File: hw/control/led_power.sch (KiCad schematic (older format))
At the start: 23 parts, among them Q1001 BC807, Q1002 BC817, U801 LM2678T-ADJ

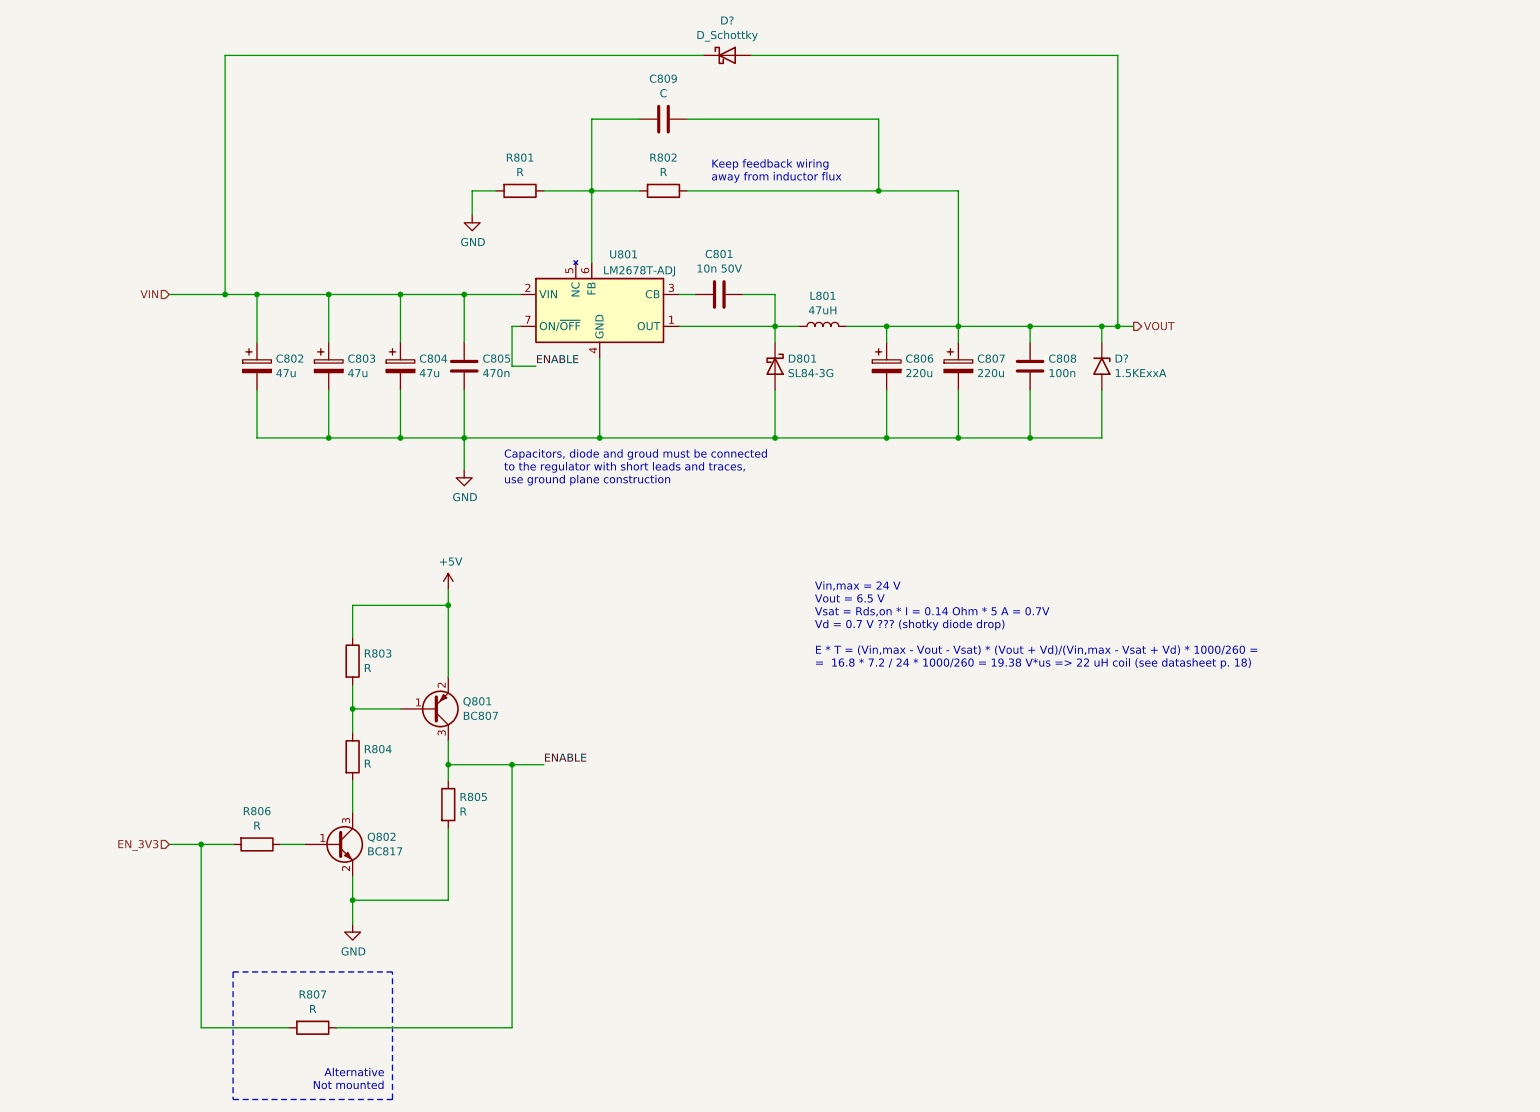
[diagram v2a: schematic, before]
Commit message: [hw] Assign control board footprints
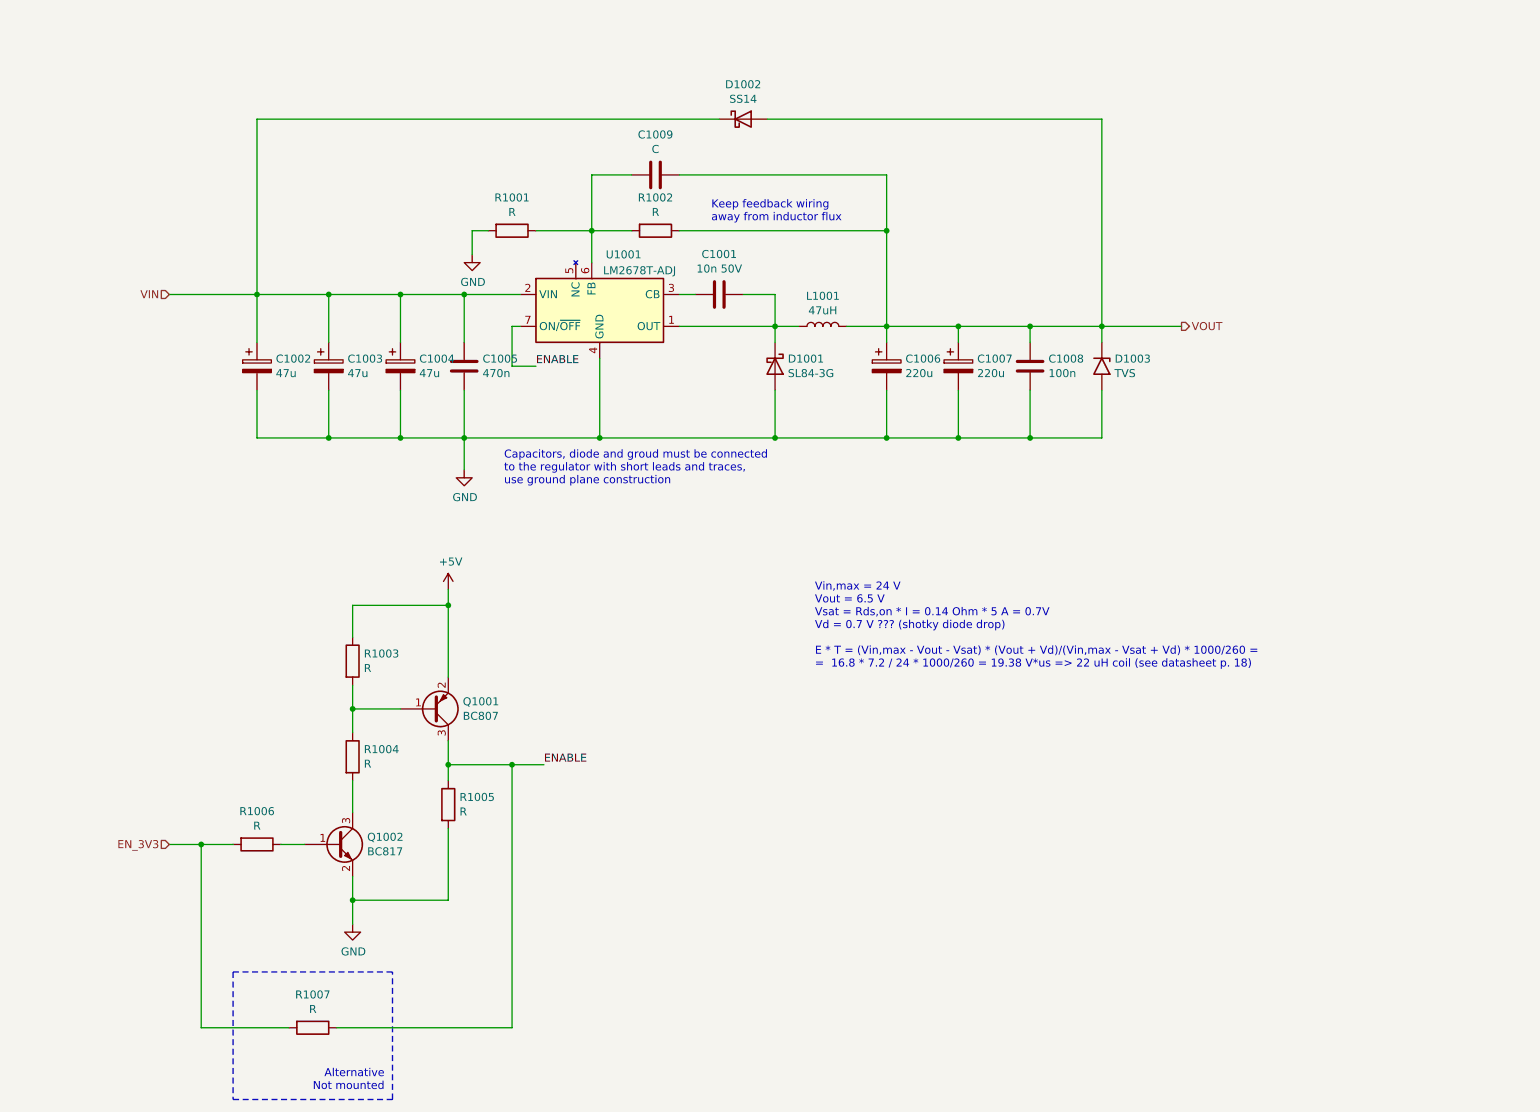
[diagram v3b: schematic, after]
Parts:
- C809: footprint (none) -> Capacitor_SMD:C_0805_2012Metric_Pad1.18x1.45mm_HandSolder
- D802: renamed from D?; value D_Schottky -> SS14; footprint (none) -> Diode_SMD:D_SMA-SMB_Universal_Handsoldering
- D803: renamed from D?; value 1.5KExxA -> TVS; footprint Diode_THT:D_DO-201AE_P15.24mm_Horizontal -> Diode_SMD:D_SMA_Handsoldering
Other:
- moved on the sheet: C1009, D1002, R1001, R1002

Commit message: [hw] Calculate some values in control board
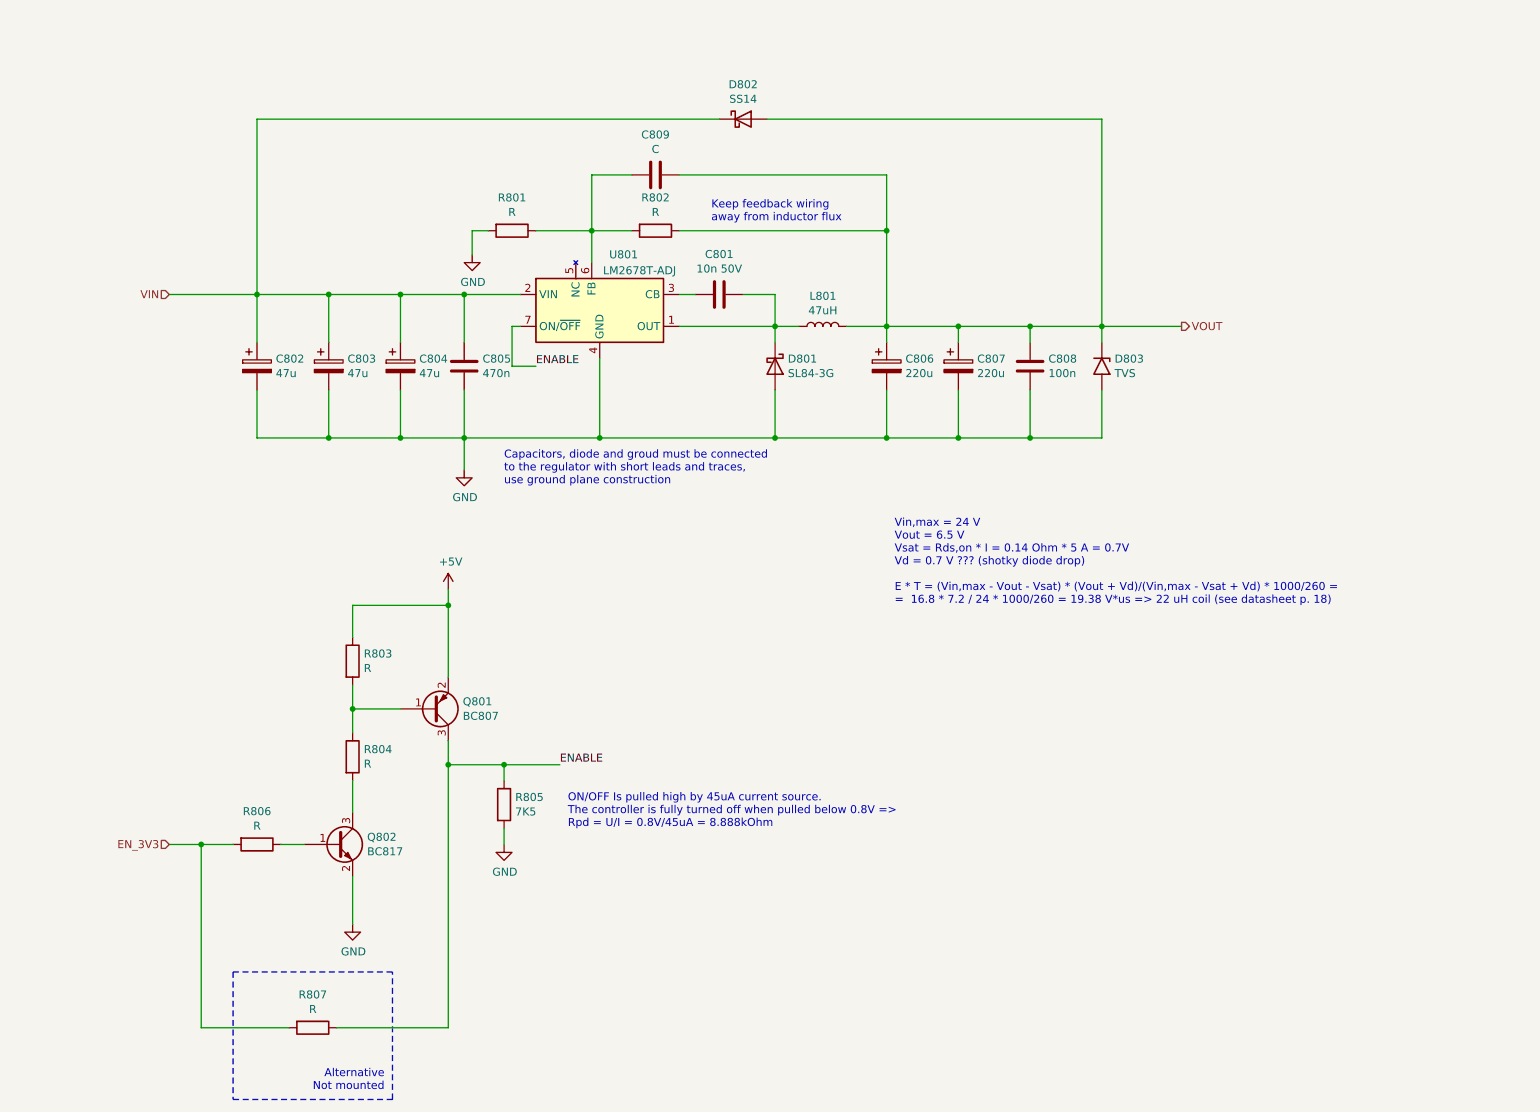
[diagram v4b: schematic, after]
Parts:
- R1005: value R -> 7K5
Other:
- note added: "ON/OFF Is pulled high by 45uA current source.\nThe controller is fully turned off when pulled below 0.8V =>\nRpd = U/I = 0.8V/45uA = 8.888kOhm"
- moved on the sheet: R805

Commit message: [hw] Update LED power supply
* Add 10 uF capacitors
* Add more space heat sinks
* Add thermal reliefs
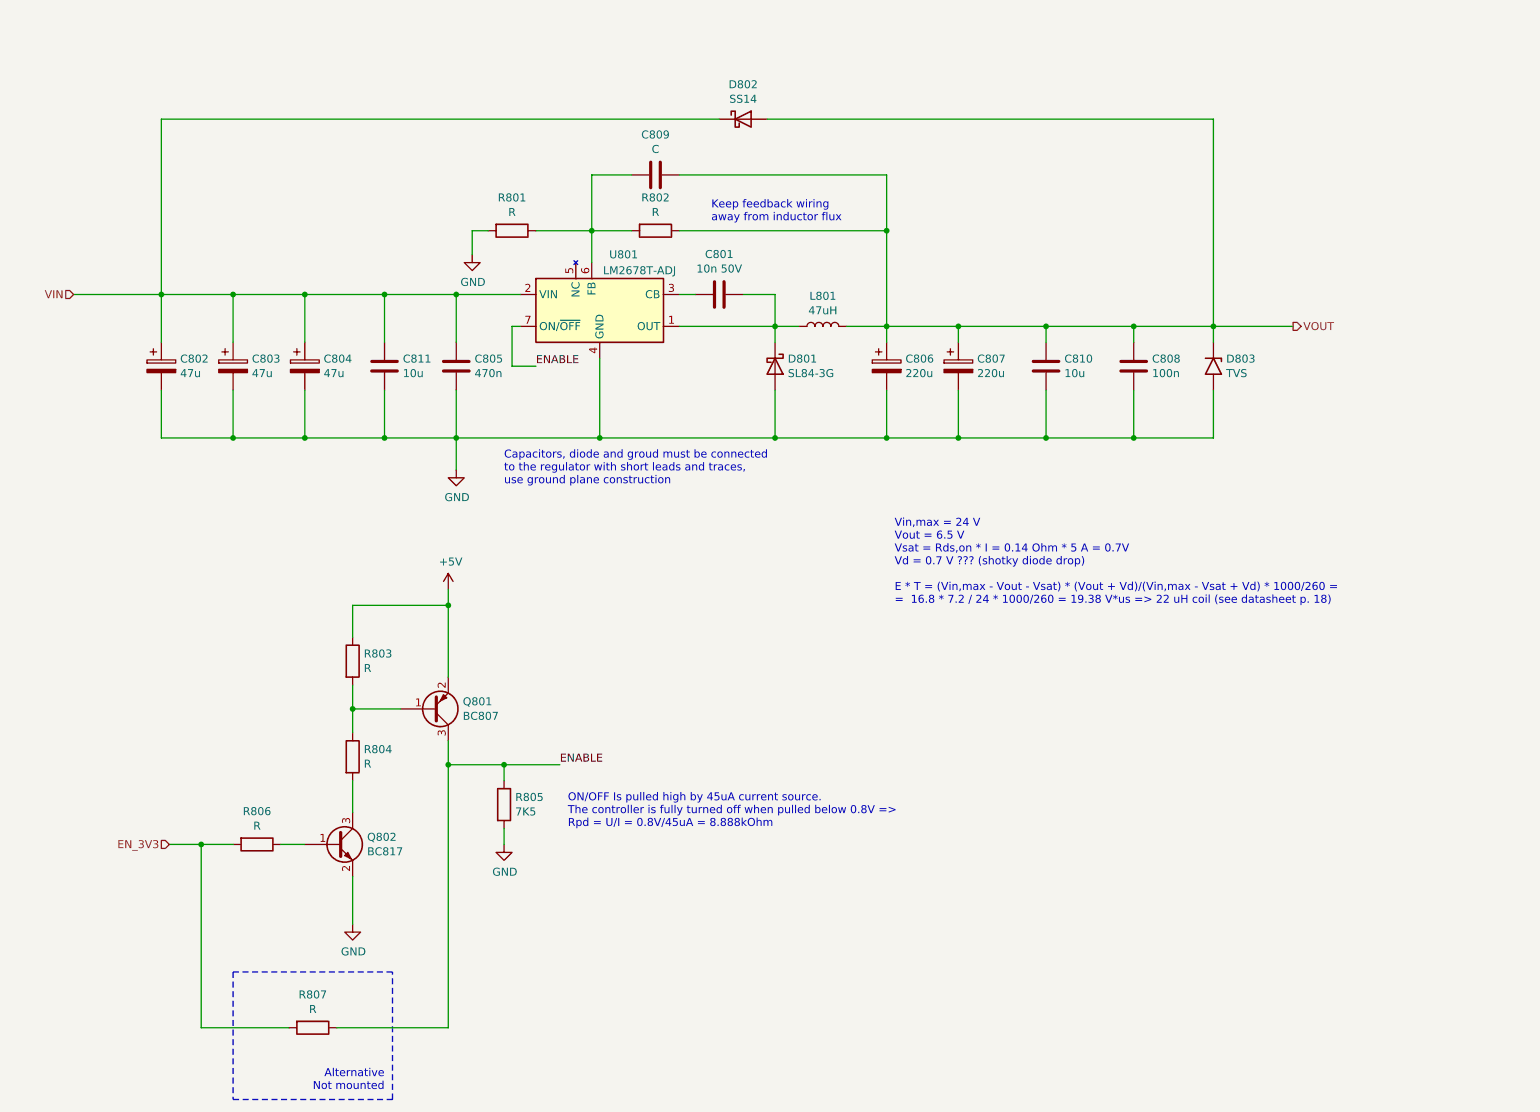
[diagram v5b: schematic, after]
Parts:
- added C810, C811: 10u, Capacitor_SMD:C_1210_3225Metric_Pad1.33x2.70mm_HandSolder, symbol Device:C
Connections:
- net GND: now also C810.2, C811.2
- net VIN: now also C811.1
- net VOUT: now also C810.1
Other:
- moved on the sheet: C802, C803, C804, C805, C808, D803
